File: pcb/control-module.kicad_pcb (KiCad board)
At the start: 2 copper layers, 78.7 x 69.9 mm, 109 parts, among them J1 Screw_Terminal_01x06, J2 Conn_01x07_Pin, J3 USB_C_Receptacle_USB2.0_16P, J4 Micro_SD_Card, P1_CONT TestPoint, P1_FIRE TestPoint, P1_GNDD TestPoint, P1_OUT TestPoint, P2_CONT TestPoint, P2_FIRE TestPoint, P2_GNDD TestPoint, P2_OUT TestPoint, Q1 SiS454DN, Q2 SiS454DN, SW1 SW_DIP_x04, U1 TPS2116DRL, U2 USBLC6-2SC6, U3 STM32U545RETxQ, U4 MS5607-02BA, U5 LSM6DSL, U6 MCP73831-2-OT, U7 MIC5504-3.3YM5

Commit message: Updated PCB
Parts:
- moved TP_SD_EJECT1 3.58 mm to (172.2, 41.2)
- moved TP_USB_D+1 0.50 mm to (180.8, 47.2)
- renumbered 3V3_{mcu} to TP_3V3_mcu1, 3V3_reg to TP_3V3_reg1, 3V3_sd to TP_3V3_sd1, BARO_CS to TP_BARO_CS1, BARO_MISO to TP_BARO_MISO1, BARO_MOSI to TP_BARO_MOSI1, BARO_SCK to TP_BARO_SCK1, BATT to TP_BATT1, BAT_{SENSE} to TP_BAT_SENSE_MID1, BOOT0 to TP_BOOT1, GND_{1} to TP_GND_1, GND_{2} to TP_GND_2, IMU_INT1 to TP_IMU_INT1, IMU_INT2 to TP_IMU_INT2, NRST to TP_NRST1, P1_CONT to TP_PYRO1_CONT1, P1_FIRE to TP_PYRO1_FIRE1, P1_GNDD to TP_PYRO1_GNDD1, P1_OUT to TP_PYRO1_OUT1, P2_CONT to TP_PYRO2_CONT1, P2_FIRE to TP_PYRO2_FIRE1, P2_GNDD to TP_PYRO2_GNDD1, P2_OUT to TP_PYRO2_OUT1, Mux_STAT to TP_Power_Mux_STAT1, SD_CLK to TP_SD_CLK1, SD_CMD to TP_SD_CMD1, SD_DAT to TP_SD_DAT1, SD_{EJECT} to TP_SD_EJECT1, SPI_CS1 to TP_SPI_CS1, SPI_MISO1 to TP_SPI_MISO1, SPI_MOSI1 to TP_SPI_MOSI1, SPI_SCK1 to TP_SPI_SCK1, USB_{D+} to TP_USB_D+1, USB_D_{-} to TP_USB_D-1, V_{USB} to TP_VUSB1, V_{USB} to TP_V_USB1, V_{BAT} to TP_V_{BAT}1, V_{mux} to TP_V_{mux}1
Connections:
- TP_USB_D+1 pad 1: /USB-C/USB_D+ -> /MCU/USB_DP
- TP_USB_D-1 pad 1: /USB-C/USB_D- -> /MCU/USB_DN
- U2 pad 4: /USB-C/USB_D+ -> /MCU/USB_DP
- U2 pad 6: /USB-C/USB_D- -> /MCU/USB_DN
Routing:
- net /BOOT0: track 19.1 -> 41.2 mm
- net /MCU/SD_DAT0: track 31.8 -> 50.1 mm
- net +5V_USB: track 2.01 -> 18.2 mm
- net /SD_EJECT: track 14.1 -> 28.5 mm, vias 2 -> 3
- net /MCU/SD_CLK: track 32.4 -> 45.5 mm
- net /NRST: track 28.2 -> 41.1 mm
- net /MCU/SD_CMD: track 29.6 -> 42.0 mm
- net GNDD: track 33.5 -> 44.2 mm, vias 35 -> 33
- net /MCU/USB_DP: track 7.20 -> 10.8 mm
- net /MCU/USB_DN: track 7.14 -> 10.4 mm
- net /MCU/VDD11: track 25.1 -> 22.6 mm, vias 3 -> 2

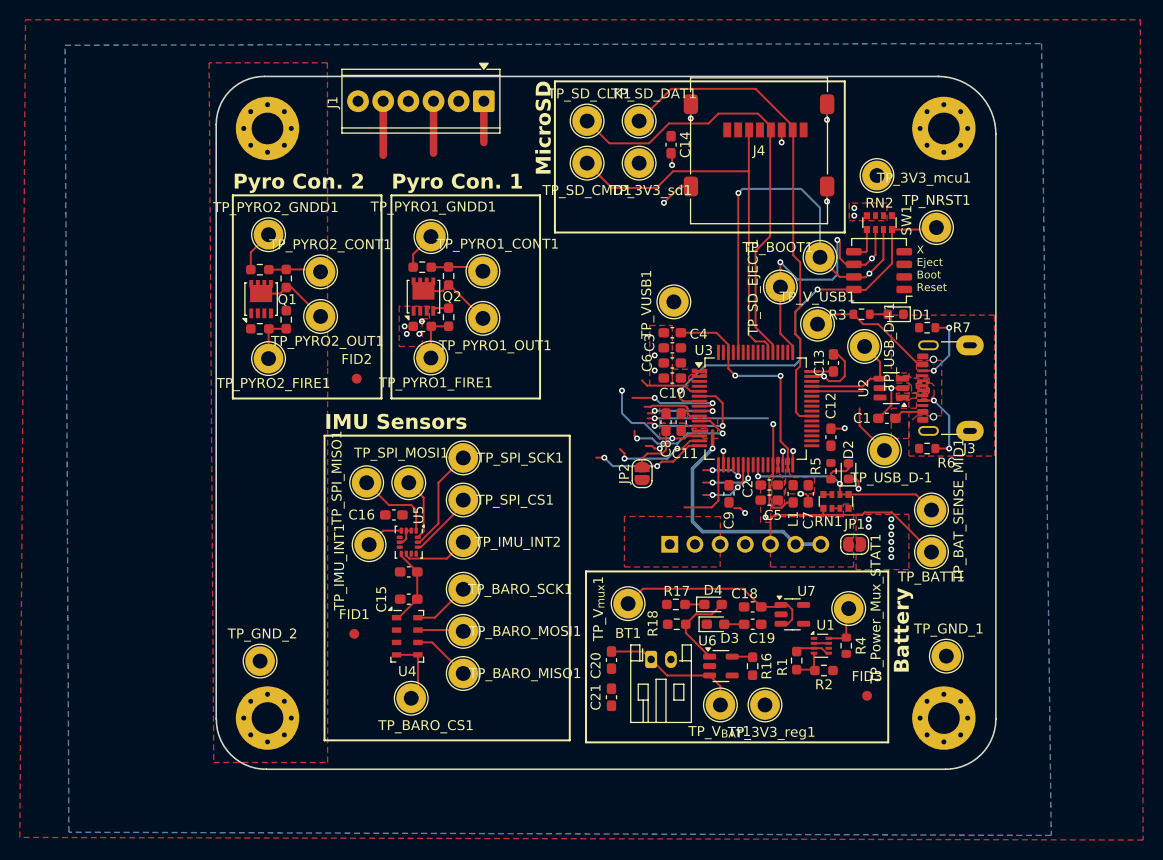
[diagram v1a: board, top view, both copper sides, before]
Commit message: Completed most of testbed layout
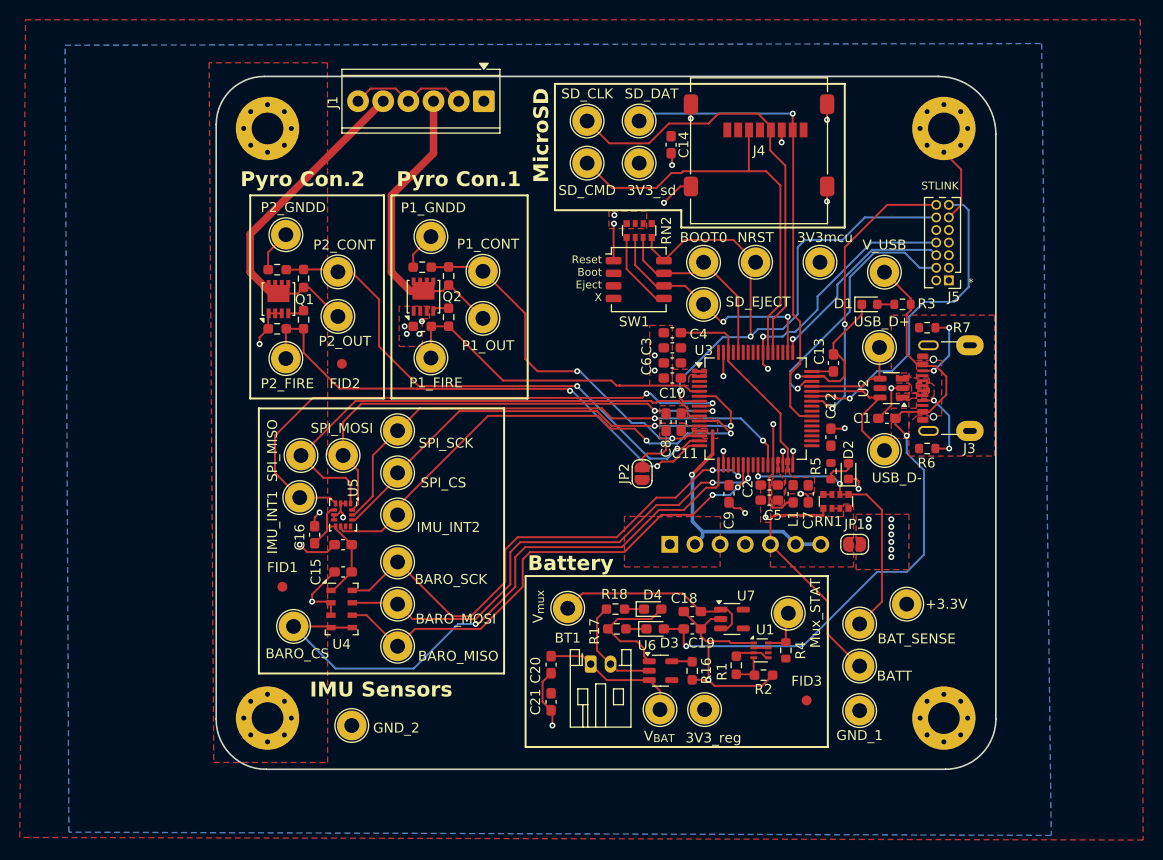
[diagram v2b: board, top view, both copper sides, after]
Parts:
- added J5: Conn_ST_STDC14, Connector_PinHeader_1.27mm:PinHeader_2x07_P1.27mm_Vertical, F.Cu at (189.2, 40.6)
- moved G*** 39.9 mm to (134.3, 28.5), turned to 180 degrees
- moved +3.3V 38.5 mm to (185.0, 73.2)
- moved SW1 24.3 mm to (158.0, 40.5), turned to 0 degrees
- moved RN2 24.3 mm to (158.0, 35.5)
- moved NRST 18.6 mm to (169.8, 38.8)
- moved BARO_CS 13.9 mm to (123.1, 75.5)
- moved BATT 13.6 mm to (180.2, 79.5)
- moved BAT_SENSE 13.6 mm to (180.2, 75.2)
- moved BOOT0 11.8 mm to (164.5, 38.8)
- moved GND_2 11.3 mm to (129.0, 85.5)
- moved 3V3mcu 10.5 mm to (176.2, 38.8)
- moved GND_1 10.3 mm to (180.2, 84.0)
- moved FID1 8.67 mm to (122.0, 71.5)
- moved V_USB 8.55 mm to (182.8, 39.8)
- moved IMU_INT1 8.46 mm to (123.8, 62.5)
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- renumbered TP_VUSB1 to +3.3V, TP_3V3_reg1 to 3V3_reg, TP_3V3_sd1 to 3V3_sd, TP_3V3_mcu1 to 3V3mcu, TP_BARO_CS1 to BARO_CS, TP_BARO_MISO1 to BARO_MISO, TP_BARO_MOSI1 to BARO_MOSI, TP_BARO_SCK1 to BARO_SCK, TP_BATT1 to BATT, TP_BAT_SENSE_MID1 to BAT_SENSE, TP_BOOT1 to BOOT0, TP_GND_1 to GND_1, TP_GND_2 to GND_2, TP_IMU_INT1 to IMU_INT1, TP_IMU_INT2 to IMU_INT2, TP_Power_Mux_STAT1 to Mux_STAT, TP_NRST1 to NRST, TP_PYRO1_CONT1 to P1_CONT, TP_PYRO1_FIRE1 to P1_FIRE, TP_PYRO1_GNDD1 to P1_GNDD, TP_PYRO1_OUT1 to P1_OUT, TP_PYRO2_CONT1 to P2_CONT, TP_PYRO2_FIRE1 to P2_FIRE, TP_PYRO2_GNDD1 to P2_GNDD, TP_PYRO2_OUT1 to P2_OUT, TP_SD_CLK1 to SD_CLK, TP_SD_CMD1 to SD_CMD, TP_SD_DAT1 to SD_DAT, TP_SD_EJECT1 to SD_EJECT, TP_SPI_CS1 to SPI_CS, TP_SPI_MISO1 to SPI_MISO, TP_SPI_MOSI1 to SPI_MOSI, TP_SPI_SCK1 to SPI_SCK, TP_USB_D+1 to USB_D+, TP_USB_D-1 to USB_D-, TP_V_USB1 to V_USB, TP_V_{BAT}1 to V_{BAT}, TP_V_{mux}1 to V_{mux}
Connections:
- U3 pad 42: unconnected-(U3-PA9-Pad42) -> /MCU/MCU_TX
- U3 pad 43: unconnected-(U3-PA10-Pad43) -> /MCU/MCU_RX
- U3 pad 46: unconnected-(U3-PA13-Pad46) -> /MCU/SWDIO
- U3 pad 49: /SD_EJECT -> /MCU/SWCLK
- U3 pad 50: unconnected-(U3-PA15-Pad50) -> /SD_EJECT
- U3 pad 55: unconnected-(U3-PB3-Pad55) -> /MCU/SWO
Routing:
- net GNDD: track 44.2 -> 125.9 mm, vias 33 -> 40
- net +5V_USB: track 18.2 -> 69.1 mm, vias 0 -> 2
- net /IMU Sensors/pres_cs: track 14.1 -> 62.1 mm, vias 0 -> 1
- net /IMU Sensors/imu_int1: track 13.6 -> 58.9 mm
- net /IMU Sensors/pres_sclk: track 10.9 -> 52.0 mm
- net /IMU Sensors/pres_mosi: track 10.6 -> 49.7 mm
- net /IMU Sensors/pres_miso: track 12.2 -> 51.1 mm
- net /MCU/ADC1_IN6: track 14.8 -> 53.1 mm
- net /IMU Sensors/imu_miso: track 14.5 -> 51.8 mm
- net /MCU/PYRO2_FIRE: track 16.4 -> 52.7 mm
- net /IMU Sensors/imu_mosi: track 14.4 -> 49.4 mm
- net /MCU/MCU_RX: track 0.00 -> 32.7 mm, vias 0 -> 1
- net /IMU Sensors/imu_int2: track 19.8 -> 50.3 mm
- net /MCU/MCU_TX: track 0.00 -> 30.2 mm, vias 0 -> 2
- net /IMU Sensors/imu_sclk: track 22.7 -> 52.3 mm, vias 1 -> 2
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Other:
- board text added: "*"
- board text added: "Pyro Con.1"
- board text added: "Pyro Con.2"
- board text added: "Reset Boot Eject X"
- board text added: "STLINK"
- board text removed: "Pyro Con. 1"
- board text removed: "Pyro Con. 2"
- board text removed: "X Eject Boot Reset"
